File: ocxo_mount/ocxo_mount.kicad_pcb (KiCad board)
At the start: 2 copper layers, 69.8 x 50.8 mm, 11 parts, among them J1 12POS 2.54MM, J2 Conn_01x12, M1 MountingPad_4-40, M2 MountingPad_4-40, M3 MountingPad_4-40, M4 MountingPad_4-40, M5 MountingPad_4-40, M6 MountingPad_4-40, M7 MountingPad_4-40, M8 MountingPad_4-40

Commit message: fix annotations
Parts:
- J1: value 12POS 2.54MM -> 12POS 2.54mm
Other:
- rule pad_to_mask_clearance: 0 -> 0.0508
- board text added: "FREQ_CTL_INPUT (0-5 VDC)"
- board text added: "JRW / JUL26 / REV A"
- board text removed: "FREQ_CTL_INPUT (0-5VDC)"
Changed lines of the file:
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@@
 	)
 	(setup
-		(pad_to_mask_clearance 0)
+		(pad_to_mask_clearance 0.0508)
+		(solder_mask_min_width 0.1016)
 		(allow_soldermask_bridges_in_footprints no)
 		(tenting
-			(front yes)
-			(back yes)
+			(front no)
+			(back no)
 		)
 		(covering
@@
 			)
 		)
-		(property "SRS P/N" "1-01602"
+		(property "MPN" "1-215299-2"
+			(at 0 0 90)
+			(unlocked yes)
+			(layer "F.Fab")
+			(hide yes)
+			(effects
+				(font
+					(size 1 1)
+					(thickness 0.15)
+				)
+			)
+		)
+		(property "SRS PN" "1-01602"
 			(at 0 0 90)
 			(unlocked yes)
@@
 			)
 		)
-		(property "Value" "12POS 2.54MM"
+		(property "Value" "12POS 2.54mm"
 			(at 7.366 -3.683 90)
 			(layer "F.Fab")
@@
 		(property "Description" "Conn Unshrouded Header HDR 12 POS 2.54mm Solder ST Thru-Hole Bulk"
 			(at 0 0 90)
-			(layer "F.Fab")
-			(hide yes)
-			(effects
-				(font
-					(size 1 1)
-					(thickness 0.15)
-				)
-			)
-		)
-		(property "Current" ""
-			(at 0 0 90)
-			(unlocked yes)
-			(layer "F.Fab")
-			(hide yes)
-			(effects
-				(font
-					(size 1 1)
-					(thickness 0.15)
-				)
-			)
-		)
-		(property "Shiny Info" ""
-			(at 0 0 90)
-			(unlocked yes)
-			(layer "F.Fab")
-			(hide yes)
-			(effects
-				(font
-					(size 1 1)
-					(thickness 0.15)
-				)
-			)
-		)
-		(property "Tempco" ""
-			(at 0 0 90)
-			(unlocked yes)
-			(layer "F.Fab")
-			(hide yes)
-			(effects
-				(font
-					(size 1 1)
-					(thickness 0.15)
-				)
-			)
-		)
-		(property "Tolerance" ""
-			(at 0 0 90)
-			(unlocked yes)
-			(layer "F.Fab")
-			(hide yes)
-			(effects
-				(font
-					(size 1 1)
-					(thickness 0.15)
-				)
-			)
-		)
-		(property "Price" "0.71"
-			(at 0 0 90)
-			(unlocked yes)
 			(layer "F.Fab")
 			(hide yes)
@@
 			)
 		)
-		(property "Footprint Modified Timestamp" "2025-10-13 21:00:08 -0800"
-			(at 0 0 90)
-			(unlocked yes)
-			(layer "F.Fab")
-			(hide yes)
-			(effects
-				(font
-					(size 1 1)
-					(thickness 0.15)
-				)
-			)
-		)
-		(property "Symbol Modified Timestamp" "2025-10-13 21:00:08 -0800"
-			(at 0 0 90)
-			(unlocked yes)
-			(layer "F.Fab")
-			(hide yes)
-			(effects
-				(font
-					(size 1 1)
-					(thickness 0.15)
-				)
-			)
-		)
-		(property "Qty In Stock" "531"
-			(at 0 0 90)
-			(unlocked yes)
-			(layer "F.Fab")
-			(hide yes)
-			(effects
-				(font
-					(size 1 1)
-					(thickness 0.15)
-				)
-			)
-		)
-		(property "Used In" "CG635,DG645,FS740,SC10L,SG382,SG382R,SG384,SG384R,SG386,SG386R,SG392,SG394,SG396"
-			(at 0 0 90)
-			(unlocked yes)
-			(layer "F.Fab")
-			(hide yes)
-			(effects
-				(font
-					(size 1 1)
-					(thickness 0.15)
-				)
-			)
-		)
-		(property "Symbol" "Connector_Generic:Conn_01x12"
-			(at 0 0 90)
-			(unlocked yes)
-			(layer "F.Fab")
-			(hide yes)
-			(effects
-				(font
-					(size 1 1)
-					(thickness 0.15)
-				)
-			)
-		)
 		(property "MPN" "HMTSW-112-22-L-S-440-LL"
 			(at 0 0 90)
@@
 		)
 		(property "Voltage" "N/A"
-			(at 0 0 90)
-			(unlocked yes)
-			(layer "F.Fab")
-			(hide yes)
-			(effects
-				(font
-					(size 1 1)
-					(thickness 0.15)
-				)
-			)
-		)
-		(property "Manf" "Samtec"
-			(at 0 0 90)
-			(unlocked yes)
-			(layer "F.Fab")
-			(hide yes)
-			(effects
-				(font
-					(size 1 1)
-					(thickness 0.15)
-				)
-			)
-		)
-		(property "Recommended" "Y"
-			(at 0 0 90)
-			(unlocked yes)
-			(layer "F.Fab")
-			(hide yes)
-			(effects
-				(font
-					(size 1 1)
-					(thickness 0.15)
-				)
-			)
-		)
-		(property "Footprint Modified By" "assignment_engine"
-			(at 0 0 90)
-			(unlocked yes)
-			(layer "F.Fab")
-			(hide yes)
-			(effects
-				(font
-					(size 1 1)
-					(thickness 0.15)
-				)
-			)
-		)
-		(property "Symbol Modified By" "assignment_engine"
 			(at 0 0 90)
 			(unlocked yes)
@@
 		)
 	)
+	(gr_text "JRW / JUL26 / REV A"
+		(at 146.5 90.5 90)
+		(layer "B.SilkS")
+		(effects
+			(font
+				(size 1.27 1.27)
+				(thickness 0.2032)
+			)
+			(justify left bottom mirror)
+		)
+	)
 	(gr_text "CONNECTED ON TARGET"
 		(at 191.008 91.948 90)
@@
 		)
 	)
-	(gr_text "FREQ_CTL_INPUT (0-5VDC)"
+	(gr_text "FREQ_CTL_INPUT (0-5 VDC)"
 		(at 157.226 94.615 180)
 		(layer "B.SilkS")

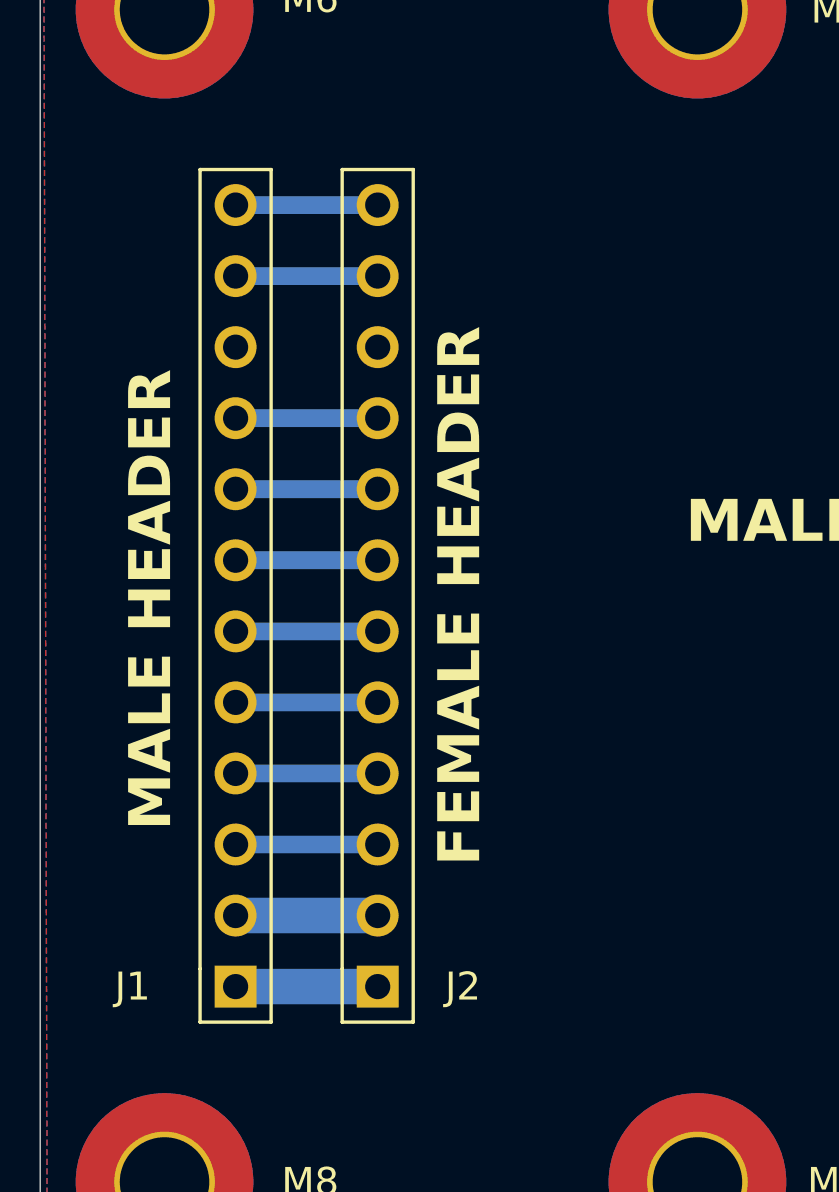
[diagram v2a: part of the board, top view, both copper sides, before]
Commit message: female header moved 5 mil away from male header
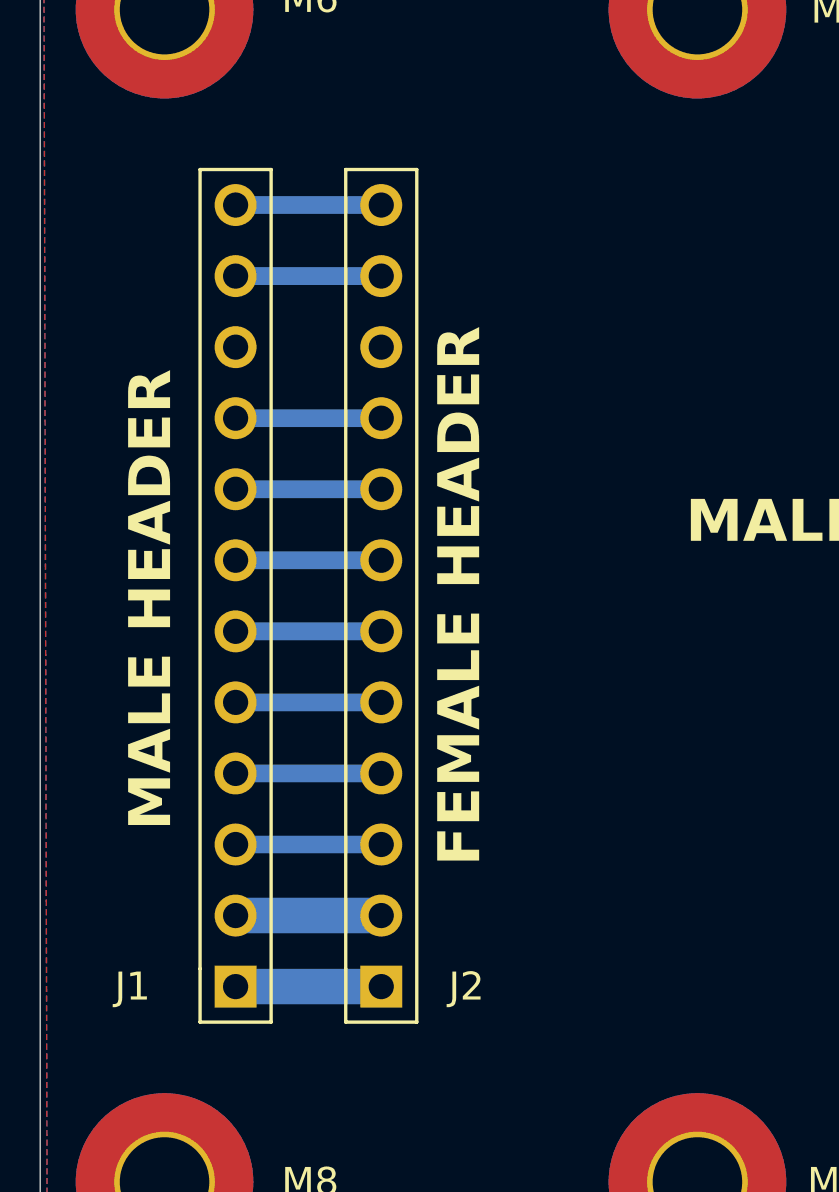
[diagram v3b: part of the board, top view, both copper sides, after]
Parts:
- moved J2 0.13 mm to (155.1, 115.6)
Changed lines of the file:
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@@
 		(capping no)
 		(filling no)
+		(aux_axis_origin 142.875 127)
 		(pcbplotparams
 			(layerselection 0x00000000_00000000_55555555_5755f5ff)
@@
 			(plotframeref no)
 			(mode 1)
-			(useauxorigin no)
+			(useauxorigin yes)
 			(pdf_front_fp_property_popups yes)
 			(pdf_back_fp_property_popups yes)
@@
 			(outputformat 1)
 			(mirror no)
-			(drillshape 1)
+			(drillshape 0)
 			(scaleselection 1)
-			(outputdirectory "")
+			(outputdirectory "gerber/")
 		)
 	)
@@
 	)
 	(footprint "CONNECTOR_SRS:HDR1X12"
-		(locked yes)
 		(layer "F.Cu")
-		(at 154.94 115.57 90)
+		(at 155.067 115.57 90)
 		(descr "Connector; Header; 12 Position")
 		(property "Reference" "J2"
@@
 		(sheetname "/")
 		(sheetfile "ocxo_mount.kicad_sch")
-		(units
-			(unit
-				(name "A")
-				(pins "1" "2" "3" "4" "5" "6" "7" "8" "9" "10" "11" "12")
-			)
-		)
 		(attr through_hole)
 		(duplicate_pad_numbers_are_jumpers no)
@@
 		)
 		(embedded_fonts no)
-		(model "${SRS_PARTS}/3dmodels/CONNECTOR_SRS.3dshapes/HDR1X12.step"
+		(model "${SRS_PARTS}/3dmodels/CONNECTOR_SRS.3dshapes/SSW-112-01-G-S.step"
 			(offset
-				(xyz 0 0 0)
+				(xyz 14 0 0)
 			)
 			(scale
@@
 			)
 			(rotate
-				(xyz 0 0 0)
+				(xyz -90 -0 -0)
 			)
 		)
@@
 		(sheetname "/")
 		(sheetfile "ocxo_mount.kicad_sch")
-		(units
-			(unit
-				(name "A")
-				(pins "1" "2" "3" "4" "5" "6" "7" "8" "9" "10" "11" "12")
-			)
-		)
 		(attr through_hole)
 		(duplicate_pad_numbers_are_jumpers no)
@@
 		)
 		(embedded_fonts no)
-		(model "${SRS_PARTS}/3dmodels/CONNECTOR_SRS.3dshapes/HDR1X12.step"
+		(model "${SRS_PARTS}/3dmodels/CONNECTOR_SRS.3dshapes/HMTSW-112-22-L-S-440-LL.step"
 			(offset
-				(xyz 0 0 0)
+				(xyz 14 0 0)
 			)
 			(scale
@@
 			)
 			(rotate
-				(xyz 0 0 0)
+				(xyz -90 -0 -0)
 			)
 		)
@@
 			(keep_text_aligned yes)
 		)
-		(gr_text "0.175"
+		(gr_text "175"
 			(at 145.0975 71.85 0)
 			(layer "F.Fab")
@@
 			(keep_text_aligned yes)
 		)
-		(gr_text "2.75"
+		(gr_text "2750"
 			(at 177.8 129.6 0)
 			(layer "F.Fab")
@@
 			(keep_text_aligned yes)
 		)
-		(gr_text "0.175"
+		(gr_text "175"
 			(at 214.85 124.7775 90)
 			(layer "F.Fab")
@@
 			(keep_text_aligned yes)
 		)
-		(gr_text "1.825"
+		(gr_text "1825"
 			(at 218.1 103.8225 90)
 			(layer "F.Fab")
@@
 			(keep_text_aligned yes)
 		)
-		(gr_text "0.45"
+		(gr_text "450"
 			(at 140.35 121.285 90)
 			(layer "F.Fab")
@@
 			(keep_text_aligned yes)
 		)
-		(gr_text "0.275"
+		(gr_text "275"
 			(at 146.3675 66.6 0)
 			(layer "F.Fab")
@@
 			(keep_text_aligned yes)
 		)
-		(gr_text "2"
+		(gr_text "2000"
 			(at 137.6 101.6 90)
 			(layer "F.Fab")
@@
 			(keep_text_aligned yes)
 		)
-		(gr_text "2.575"
+		(gr_text "2575"
 			(at 175.5775 61.85 0)
 			(layer "F.Fab")
